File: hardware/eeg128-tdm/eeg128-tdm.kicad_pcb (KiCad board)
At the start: 4 copper layers, 190 x 110 mm, 642 parts, among them J1 J1, J10 J10, J11 J11, J2 J2, J3 J3, J4 J4, J5 J5, J6 J6, J7 J7, J8 J8, J9 TYPE-C-31-M-12, U1 U1, U10 U10, U11 U11, U12 U12, U13 U13, U14 U14, U15 U15, U16 U16, U17 U17, U18 U18, U19 U19, U2 U2, U20 U20, U21 U21, U22 U22, U23 U23, U24 U24, U25 U25, U26 U26, U27 U27, U3 U3, U4 U4, U5 U5, U6 U6, U7 U7, U8 U8, U9 U9, Y1 Y1

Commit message: Materialize generated KiCad schematic and release manifest
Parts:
- U21: footprint LQFP-32_5x5mm_P0.5mm -> TI_PBS_S-PQFP-G32_5x5mm_P0.5mm

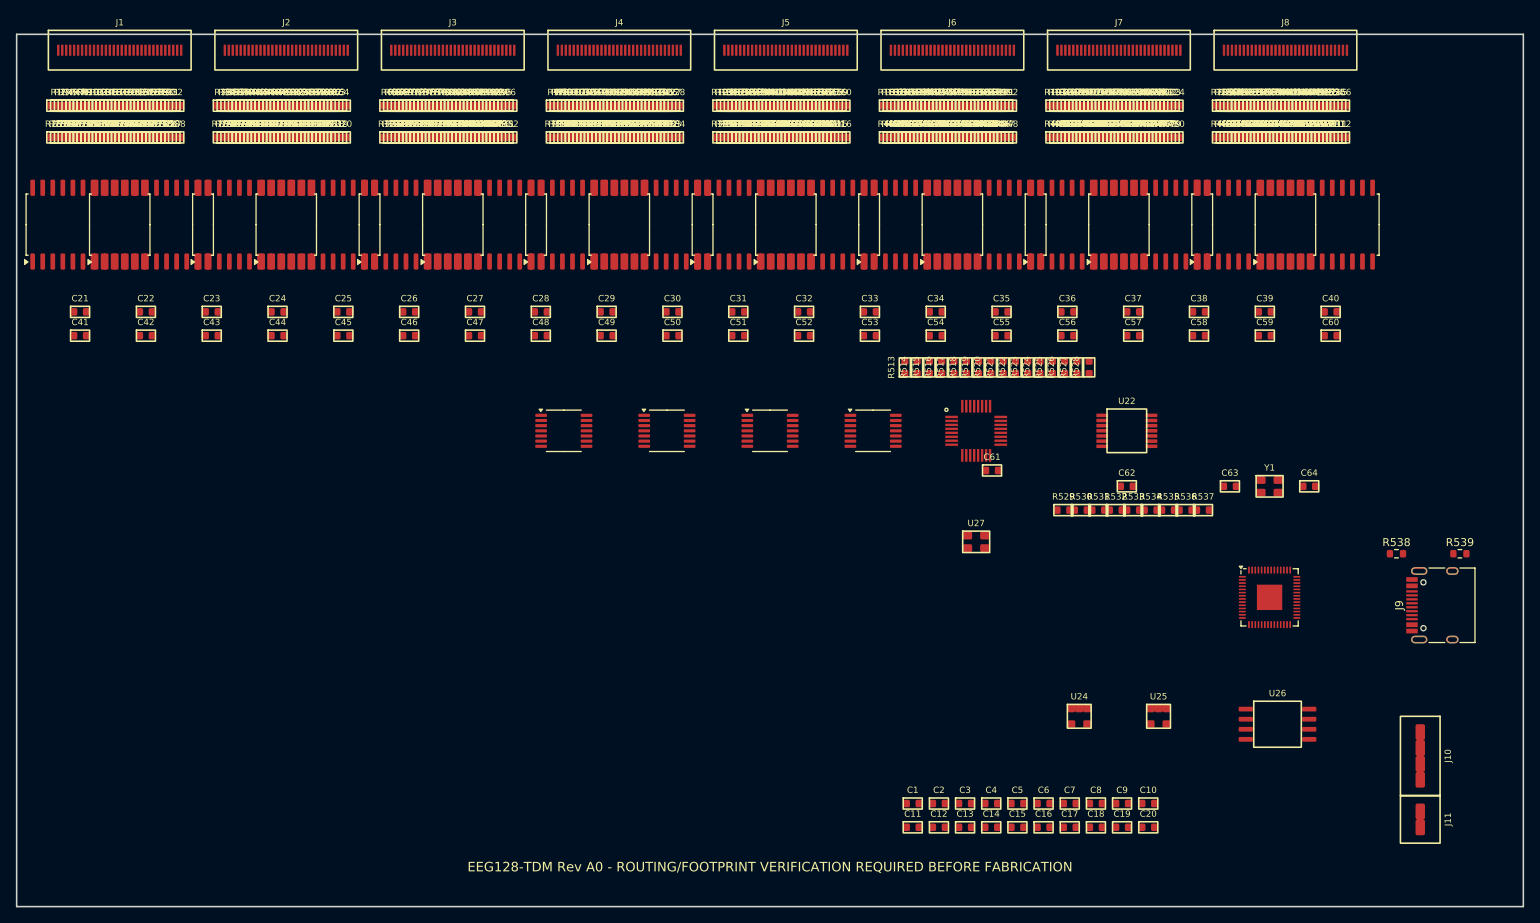
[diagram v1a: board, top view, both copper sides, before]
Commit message: Materialize verified pre-route PCB and gate primary geometry
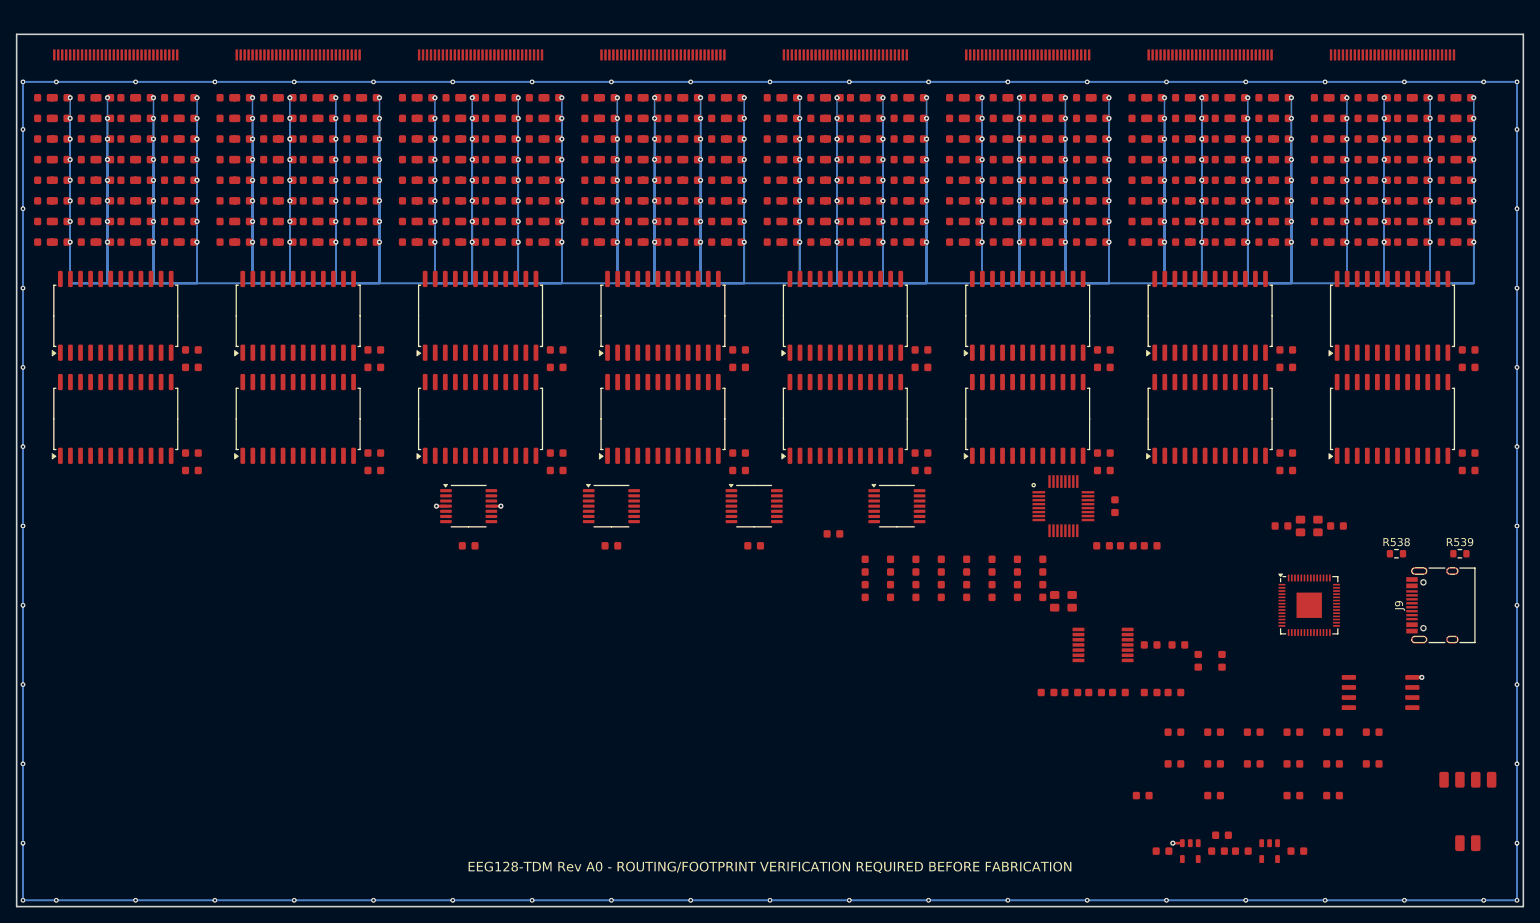
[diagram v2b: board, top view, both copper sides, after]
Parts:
- C1: footprint NBFM1_A0:C1 -> C1
- C10: footprint NBFM1_A0:C10 -> C10
- C11: footprint NBFM1_A0:C11 -> C11
- C12: footprint NBFM1_A0:C12 -> C12
- C13: footprint NBFM1_A0:C13 -> C13
- C14: footprint NBFM1_A0:C14 -> C14
- C15: footprint NBFM1_A0:C15 -> C15
- C16: footprint NBFM1_A0:C16 -> C16
- C17: footprint NBFM1_A0:C17 -> C17
- C18: footprint NBFM1_A0:C18 -> C18
- C19: footprint NBFM1_A0:C19 -> C19
- C2: footprint NBFM1_A0:C2 -> C2
- C20: footprint NBFM1_A0:C20 -> C20
- C21: footprint NBFM1_A0:C21 -> C21
- C22: footprint NBFM1_A0:C22 -> C22
- C23: footprint NBFM1_A0:C23 -> C23
- C24: footprint NBFM1_A0:C24 -> C24
- C25: footprint NBFM1_A0:C25 -> C25
- C26: footprint NBFM1_A0:C26 -> C26
- C27: footprint NBFM1_A0:C27 -> C27
- C28: footprint NBFM1_A0:C28 -> C28
- C29: footprint NBFM1_A0:C29 -> C29
- C3: footprint NBFM1_A0:C3 -> C3
- C30: footprint NBFM1_A0:C30 -> C30
- C31: footprint NBFM1_A0:C31 -> C31
- C32: footprint NBFM1_A0:C32 -> C32
- C33: footprint NBFM1_A0:C33 -> C33
- C34: footprint NBFM1_A0:C34 -> C34
- C35: footprint NBFM1_A0:C35 -> C35
- C36: footprint NBFM1_A0:C36 -> C36
- C37: footprint NBFM1_A0:C37 -> C37
- C38: footprint NBFM1_A0:C38 -> C38
- C39: footprint NBFM1_A0:C39 -> C39
- C4: footprint NBFM1_A0:C4 -> C4
- C40: footprint NBFM1_A0:C40 -> C40
- C41: footprint NBFM1_A0:C41 -> C41
- C42: footprint NBFM1_A0:C42 -> C42
- C43: footprint NBFM1_A0:C43 -> C43
- C44: footprint NBFM1_A0:C44 -> C44
- C45: footprint NBFM1_A0:C45 -> C45
- C46: footprint NBFM1_A0:C46 -> C46
- C47: footprint NBFM1_A0:C47 -> C47
- C48: footprint NBFM1_A0:C48 -> C48
- C49: footprint NBFM1_A0:C49 -> C49
- C5: footprint NBFM1_A0:C5 -> C5
- C50: footprint NBFM1_A0:C50 -> C50
- C51: footprint NBFM1_A0:C51 -> C51
- C52: footprint NBFM1_A0:C52 -> C52
- C53: footprint NBFM1_A0:C53 -> C53
- C54: footprint NBFM1_A0:C54 -> C54
- C55: footprint NBFM1_A0:C55 -> C55
- C56: footprint NBFM1_A0:C56 -> C56
- C57: footprint NBFM1_A0:C57 -> C57
- C58: footprint NBFM1_A0:C58 -> C58
- C59: footprint NBFM1_A0:C59 -> C59
- C6: footprint NBFM1_A0:C6 -> C6
- C60: footprint NBFM1_A0:C60 -> C60
- C61: footprint NBFM1_A0:C61 -> C61
- C62: footprint NBFM1_A0:C62 -> C62
- C63: footprint NBFM1_A0:C63 -> C63
- C64: footprint NBFM1_A0:C64 -> C64
- C7: footprint NBFM1_A0:C7 -> C7
- C8: footprint NBFM1_A0:C8 -> C8
- C9: footprint NBFM1_A0:C9 -> C9
- J1: footprint NBFM1_A0:J1 -> J1
- J10: footprint NBFM1_A0:J10 -> J10
- J11: footprint NBFM1_A0:J11 -> J11
- J2: footprint NBFM1_A0:J2 -> J2
- J3: footprint NBFM1_A0:J3 -> J3
- J4: footprint NBFM1_A0:J4 -> J4
- J5: footprint NBFM1_A0:J5 -> J5
- J6: footprint NBFM1_A0:J6 -> J6
- J7: footprint NBFM1_A0:J7 -> J7
- J8: footprint NBFM1_A0:J8 -> J8
- R1: footprint NBFM1_A0:R1 -> R1
- R10: footprint NBFM1_A0:R10 -> R10
- R100: footprint NBFM1_A0:R100 -> R100
- R101: footprint NBFM1_A0:R101 -> R101
- R102: footprint NBFM1_A0:R102 -> R102
- R103: footprint NBFM1_A0:R103 -> R103
- R104: footprint NBFM1_A0:R104 -> R104
- R105: footprint NBFM1_A0:R105 -> R105
- R106: footprint NBFM1_A0:R106 -> R106
- R107: footprint NBFM1_A0:R107 -> R107
- R108: footprint NBFM1_A0:R108 -> R108
- R109: footprint NBFM1_A0:R109 -> R109
- R11: footprint NBFM1_A0:R11 -> R11
- R110: footprint NBFM1_A0:R110 -> R110
- R111: footprint NBFM1_A0:R111 -> R111
- R112: footprint NBFM1_A0:R112 -> R112
- R113: footprint NBFM1_A0:R113 -> R113
- R114: footprint NBFM1_A0:R114 -> R114
- R115: footprint NBFM1_A0:R115 -> R115
- R116: footprint NBFM1_A0:R116 -> R116
- R117: footprint NBFM1_A0:R117 -> R117
- R118: footprint NBFM1_A0:R118 -> R118
- R119: footprint NBFM1_A0:R119 -> R119
- R12: footprint NBFM1_A0:R12 -> R12
- R120: footprint NBFM1_A0:R120 -> R120
- R121: footprint NBFM1_A0:R121 -> R121
- R122: footprint NBFM1_A0:R122 -> R122
- R123: footprint NBFM1_A0:R123 -> R123
- R124: footprint NBFM1_A0:R124 -> R124
- R125: footprint NBFM1_A0:R125 -> R125
- R126: footprint NBFM1_A0:R126 -> R126
- R127: footprint NBFM1_A0:R127 -> R127
- R128: footprint NBFM1_A0:R128 -> R128
- R129: footprint NBFM1_A0:R129 -> R129
- R13: footprint NBFM1_A0:R13 -> R13
- R130: footprint NBFM1_A0:R130 -> R130
- R131: footprint NBFM1_A0:R131 -> R131
- R132: footprint NBFM1_A0:R132 -> R132
- R133: footprint NBFM1_A0:R133 -> R133
- R134: footprint NBFM1_A0:R134 -> R134
- R135: footprint NBFM1_A0:R135 -> R135
- R136: footprint NBFM1_A0:R136 -> R136
- R137: footprint NBFM1_A0:R137 -> R137
- R138: footprint NBFM1_A0:R138 -> R138
- R139: footprint NBFM1_A0:R139 -> R139
- R14: footprint NBFM1_A0:R14 -> R14
- R140: footprint NBFM1_A0:R140 -> R140
- R141: footprint NBFM1_A0:R141 -> R141
- R142: footprint NBFM1_A0:R142 -> R142
- R143: footprint NBFM1_A0:R143 -> R143
- R144: footprint NBFM1_A0:R144 -> R144
- R145: footprint NBFM1_A0:R145 -> R145
- R146: footprint NBFM1_A0:R146 -> R146
- R147: footprint NBFM1_A0:R147 -> R147
- R148: footprint NBFM1_A0:R148 -> R148
- R149: footprint NBFM1_A0:R149 -> R149
- R15: footprint NBFM1_A0:R15 -> R15
- R150: footprint NBFM1_A0:R150 -> R150
- R151: footprint NBFM1_A0:R151 -> R151
- R152: footprint NBFM1_A0:R152 -> R152
- R153: footprint NBFM1_A0:R153 -> R153
- R154: footprint NBFM1_A0:R154 -> R154
- R155: footprint NBFM1_A0:R155 -> R155
- R156: footprint NBFM1_A0:R156 -> R156
- R157: footprint NBFM1_A0:R157 -> R157
- R158: footprint NBFM1_A0:R158 -> R158
- R159: footprint NBFM1_A0:R159 -> R159
- R16: footprint NBFM1_A0:R16 -> R16
- R160: footprint NBFM1_A0:R160 -> R160
- R161: footprint NBFM1_A0:R161 -> R161
- R162: footprint NBFM1_A0:R162 -> R162
- R163: footprint NBFM1_A0:R163 -> R163
- R164: footprint NBFM1_A0:R164 -> R164
- R165: footprint NBFM1_A0:R165 -> R165
- R166: footprint NBFM1_A0:R166 -> R166
- R167: footprint NBFM1_A0:R167 -> R167
- R168: footprint NBFM1_A0:R168 -> R168
- R169: footprint NBFM1_A0:R169 -> R169
- R17: footprint NBFM1_A0:R17 -> R17
- R170: footprint NBFM1_A0:R170 -> R170
- R171: footprint NBFM1_A0:R171 -> R171
- R172: footprint NBFM1_A0:R172 -> R172
- R173: footprint NBFM1_A0:R173 -> R173
- R174: footprint NBFM1_A0:R174 -> R174
- R175: footprint NBFM1_A0:R175 -> R175
- R176: footprint NBFM1_A0:R176 -> R176
- R177: footprint NBFM1_A0:R177 -> R177
- R178: footprint NBFM1_A0:R178 -> R178
- R179: footprint NBFM1_A0:R179 -> R179
- R18: footprint NBFM1_A0:R18 -> R18
- R180: footprint NBFM1_A0:R180 -> R180
- R181: footprint NBFM1_A0:R181 -> R181
- R182: footprint NBFM1_A0:R182 -> R182
- R183: footprint NBFM1_A0:R183 -> R183
- R184: footprint NBFM1_A0:R184 -> R184
- R185: footprint NBFM1_A0:R185 -> R185
- R186: footprint NBFM1_A0:R186 -> R186
- R187: footprint NBFM1_A0:R187 -> R187
- R188: footprint NBFM1_A0:R188 -> R188
- R189: footprint NBFM1_A0:R189 -> R189
- R19: footprint NBFM1_A0:R19 -> R19
- R190: footprint NBFM1_A0:R190 -> R190
- R191: footprint NBFM1_A0:R191 -> R191
- R192: footprint NBFM1_A0:R192 -> R192
- R193: footprint NBFM1_A0:R193 -> R193
- R194: footprint NBFM1_A0:R194 -> R194
- R195: footprint NBFM1_A0:R195 -> R195
- R196: footprint NBFM1_A0:R196 -> R196
- R197: footprint NBFM1_A0:R197 -> R197
- R198: footprint NBFM1_A0:R198 -> R198
- R199: footprint NBFM1_A0:R199 -> R199
- R2: footprint NBFM1_A0:R2 -> R2
- R20: footprint NBFM1_A0:R20 -> R20
- R200: footprint NBFM1_A0:R200 -> R200
- R201: footprint NBFM1_A0:R201 -> R201
- R202: footprint NBFM1_A0:R202 -> R202
- R203: footprint NBFM1_A0:R203 -> R203
- R204: footprint NBFM1_A0:R204 -> R204
- R205: footprint NBFM1_A0:R205 -> R205
- R206: footprint NBFM1_A0:R206 -> R206
- R207: footprint NBFM1_A0:R207 -> R207
- R208: footprint NBFM1_A0:R208 -> R208
- R209: footprint NBFM1_A0:R209 -> R209
- R21: footprint NBFM1_A0:R21 -> R21
- R210: footprint NBFM1_A0:R210 -> R210
- R211: footprint NBFM1_A0:R211 -> R211
- R212: footprint NBFM1_A0:R212 -> R212
- R213: footprint NBFM1_A0:R213 -> R213
- R214: footprint NBFM1_A0:R214 -> R214
- R215: footprint NBFM1_A0:R215 -> R215
- R216: footprint NBFM1_A0:R216 -> R216
- R217: footprint NBFM1_A0:R217 -> R217
- R218: footprint NBFM1_A0:R218 -> R218
- R219: footprint NBFM1_A0:R219 -> R219
- R22: footprint NBFM1_A0:R22 -> R22
- R220: footprint NBFM1_A0:R220 -> R220
- R221: footprint NBFM1_A0:R221 -> R221
- R222: footprint NBFM1_A0:R222 -> R222
- R223: footprint NBFM1_A0:R223 -> R223
- R224: footprint NBFM1_A0:R224 -> R224
- R225: footprint NBFM1_A0:R225 -> R225
- R226: footprint NBFM1_A0:R226 -> R226
- R227: footprint NBFM1_A0:R227 -> R227
- R228: footprint NBFM1_A0:R228 -> R228
- R229: footprint NBFM1_A0:R229 -> R229
- R23: footprint NBFM1_A0:R23 -> R23
- R230: footprint NBFM1_A0:R230 -> R230
- R231: footprint NBFM1_A0:R231 -> R231
- R232: footprint NBFM1_A0:R232 -> R232
- R233: footprint NBFM1_A0:R233 -> R233
- R234: footprint NBFM1_A0:R234 -> R234
- R235: footprint NBFM1_A0:R235 -> R235
- R236: footprint NBFM1_A0:R236 -> R236
- R237: footprint NBFM1_A0:R237 -> R237
- R238: footprint NBFM1_A0:R238 -> R238
- R239: footprint NBFM1_A0:R239 -> R239
- R24: footprint NBFM1_A0:R24 -> R24
- R240: footprint NBFM1_A0:R240 -> R240
- R241: footprint NBFM1_A0:R241 -> R241
- R242: footprint NBFM1_A0:R242 -> R242
- R243: footprint NBFM1_A0:R243 -> R243
- R244: footprint NBFM1_A0:R244 -> R244
- R245: footprint NBFM1_A0:R245 -> R245
- R246: footprint NBFM1_A0:R246 -> R246
- R247: footprint NBFM1_A0:R247 -> R247
- R248: footprint NBFM1_A0:R248 -> R248
- R249: footprint NBFM1_A0:R249 -> R249
- R25: footprint NBFM1_A0:R25 -> R25
- R250: footprint NBFM1_A0:R250 -> R250
- R251: footprint NBFM1_A0:R251 -> R251
- R252: footprint NBFM1_A0:R252 -> R252
- R253: footprint NBFM1_A0:R253 -> R253
- R254: footprint NBFM1_A0:R254 -> R254
- R255: footprint NBFM1_A0:R255 -> R255
- R256: footprint NBFM1_A0:R256 -> R256
- R257: footprint NBFM1_A0:R257 -> R257
- R258: footprint NBFM1_A0:R258 -> R258
- R259: footprint NBFM1_A0:R259 -> R259
- R26: footprint NBFM1_A0:R26 -> R26
- R260: footprint NBFM1_A0:R260 -> R260
- R261: footprint NBFM1_A0:R261 -> R261
- R262: footprint NBFM1_A0:R262 -> R262
- R263: footprint NBFM1_A0:R263 -> R263
- R264: footprint NBFM1_A0:R264 -> R264
- R265: footprint NBFM1_A0:R265 -> R265
- R266: footprint NBFM1_A0:R266 -> R266
- R267: footprint NBFM1_A0:R267 -> R267
- R268: footprint NBFM1_A0:R268 -> R268
- R269: footprint NBFM1_A0:R269 -> R269
- R27: footprint NBFM1_A0:R27 -> R27
- R270: footprint NBFM1_A0:R270 -> R270
- R271: footprint NBFM1_A0:R271 -> R271
- R272: footprint NBFM1_A0:R272 -> R272
- R273: footprint NBFM1_A0:R273 -> R273
- R274: footprint NBFM1_A0:R274 -> R274
- R275: footprint NBFM1_A0:R275 -> R275
- R276: footprint NBFM1_A0:R276 -> R276
- R277: footprint NBFM1_A0:R277 -> R277
- R278: footprint NBFM1_A0:R278 -> R278
- R279: footprint NBFM1_A0:R279 -> R279
- R28: footprint NBFM1_A0:R28 -> R28
- R280: footprint NBFM1_A0:R280 -> R280
- R281: footprint NBFM1_A0:R281 -> R281
- R282: footprint NBFM1_A0:R282 -> R282
- R283: footprint NBFM1_A0:R283 -> R283
- R284: footprint NBFM1_A0:R284 -> R284
- R285: footprint NBFM1_A0:R285 -> R285
- R286: footprint NBFM1_A0:R286 -> R286
- R287: footprint NBFM1_A0:R287 -> R287
- R288: footprint NBFM1_A0:R288 -> R288
- R289: footprint NBFM1_A0:R289 -> R289
- R29: footprint NBFM1_A0:R29 -> R29
- R290: footprint NBFM1_A0:R290 -> R290
- R291: footprint NBFM1_A0:R291 -> R291
- R292: footprint NBFM1_A0:R292 -> R292
- R293: footprint NBFM1_A0:R293 -> R293
- R294: footprint NBFM1_A0:R294 -> R294
- R295: footprint NBFM1_A0:R295 -> R295
- R296: footprint NBFM1_A0:R296 -> R296
- R297: footprint NBFM1_A0:R297 -> R297
- R298: footprint NBFM1_A0:R298 -> R298
- R299: footprint NBFM1_A0:R299 -> R299
- R3: footprint NBFM1_A0:R3 -> R3
- R30: footprint NBFM1_A0:R30 -> R30
- R300: footprint NBFM1_A0:R300 -> R300
- R301: footprint NBFM1_A0:R301 -> R301
- R302: footprint NBFM1_A0:R302 -> R302
- R303: footprint NBFM1_A0:R303 -> R303
- R304: footprint NBFM1_A0:R304 -> R304
- R305: footprint NBFM1_A0:R305 -> R305
- R306: footprint NBFM1_A0:R306 -> R306
- R307: footprint NBFM1_A0:R307 -> R307
- R308: footprint NBFM1_A0:R308 -> R308
- R309: footprint NBFM1_A0:R309 -> R309
- R31: footprint NBFM1_A0:R31 -> R31
- R310: footprint NBFM1_A0:R310 -> R310
- R311: footprint NBFM1_A0:R311 -> R311
- R312: footprint NBFM1_A0:R312 -> R312
- R313: footprint NBFM1_A0:R313 -> R313
- R314: footprint NBFM1_A0:R314 -> R314
- R315: footprint NBFM1_A0:R315 -> R315
- R316: footprint NBFM1_A0:R316 -> R316
- R317: footprint NBFM1_A0:R317 -> R317
- R318: footprint NBFM1_A0:R318 -> R318
- R319: footprint NBFM1_A0:R319 -> R319
- R32: footprint NBFM1_A0:R32 -> R32
- R320: footprint NBFM1_A0:R320 -> R320
- R321: footprint NBFM1_A0:R321 -> R321
- R322: footprint NBFM1_A0:R322 -> R322
- R323: footprint NBFM1_A0:R323 -> R323
- R324: footprint NBFM1_A0:R324 -> R324
- R325: footprint NBFM1_A0:R325 -> R325
- R326: footprint NBFM1_A0:R326 -> R326
- R327: footprint NBFM1_A0:R327 -> R327
- R328: footprint NBFM1_A0:R328 -> R328
- R329: footprint NBFM1_A0:R329 -> R329
- R33: footprint NBFM1_A0:R33 -> R33
- R330: footprint NBFM1_A0:R330 -> R330
- R331: footprint NBFM1_A0:R331 -> R331
- R332: footprint NBFM1_A0:R332 -> R332
- R333: footprint NBFM1_A0:R333 -> R333
- R334: footprint NBFM1_A0:R334 -> R334
- R335: footprint NBFM1_A0:R335 -> R335
- R336: footprint NBFM1_A0:R336 -> R336
- R337: footprint NBFM1_A0:R337 -> R337
- R338: footprint NBFM1_A0:R338 -> R338
- R339: footprint NBFM1_A0:R339 -> R339
- R34: footprint NBFM1_A0:R34 -> R34
- R340: footprint NBFM1_A0:R340 -> R340
- R341: footprint NBFM1_A0:R341 -> R341
- R342: footprint NBFM1_A0:R342 -> R342
- R343: footprint NBFM1_A0:R343 -> R343
- R344: footprint NBFM1_A0:R344 -> R344
- R345: footprint NBFM1_A0:R345 -> R345
- R346: footprint NBFM1_A0:R346 -> R346
- R347: footprint NBFM1_A0:R347 -> R347
- R348: footprint NBFM1_A0:R348 -> R348
- R349: footprint NBFM1_A0:R349 -> R349
- R35: footprint NBFM1_A0:R35 -> R35
- R350: footprint NBFM1_A0:R350 -> R350
- R351: footprint NBFM1_A0:R351 -> R351
- R352: footprint NBFM1_A0:R352 -> R352
- R353: footprint NBFM1_A0:R353 -> R353
- R354: footprint NBFM1_A0:R354 -> R354
- R355: footprint NBFM1_A0:R355 -> R355
- R356: footprint NBFM1_A0:R356 -> R356
- R357: footprint NBFM1_A0:R357 -> R357
- R358: footprint NBFM1_A0:R358 -> R358
- R359: footprint NBFM1_A0:R359 -> R359
- R36: footprint NBFM1_A0:R36 -> R36
- R360: footprint NBFM1_A0:R360 -> R360
- R361: footprint NBFM1_A0:R361 -> R361
- R362: footprint NBFM1_A0:R362 -> R362
- R363: footprint NBFM1_A0:R363 -> R363
- R364: footprint NBFM1_A0:R364 -> R364
- R365: footprint NBFM1_A0:R365 -> R365
- R366: footprint NBFM1_A0:R366 -> R366
- R367: footprint NBFM1_A0:R367 -> R367
- R368: footprint NBFM1_A0:R368 -> R368
- R369: footprint NBFM1_A0:R369 -> R369
- R37: footprint NBFM1_A0:R37 -> R37
- R370: footprint NBFM1_A0:R370 -> R370
- R371: footprint NBFM1_A0:R371 -> R371
- R372: footprint NBFM1_A0:R372 -> R372
- R373: footprint NBFM1_A0:R373 -> R373
- R374: footprint NBFM1_A0:R374 -> R374
- R375: footprint NBFM1_A0:R375 -> R375
- R376: footprint NBFM1_A0:R376 -> R376
- R377: footprint NBFM1_A0:R377 -> R377
- R378: footprint NBFM1_A0:R378 -> R378
- R379: footprint NBFM1_A0:R379 -> R379
- R38: footprint NBFM1_A0:R38 -> R38
- R380: footprint NBFM1_A0:R380 -> R380
- R381: footprint NBFM1_A0:R381 -> R381
- R382: footprint NBFM1_A0:R382 -> R382
- R383: footprint NBFM1_A0:R383 -> R383
- R384: footprint NBFM1_A0:R384 -> R384
- R385: footprint NBFM1_A0:R385 -> R385
- R386: footprint NBFM1_A0:R386 -> R386
- R387: footprint NBFM1_A0:R387 -> R387
- R388: footprint NBFM1_A0:R388 -> R388
- R389: footprint NBFM1_A0:R389 -> R389
- R39: footprint NBFM1_A0:R39 -> R39
- R390: footprint NBFM1_A0:R390 -> R390
- R391: footprint NBFM1_A0:R391 -> R391
- R392: footprint NBFM1_A0:R392 -> R392
- R393: footprint NBFM1_A0:R393 -> R393
- R394: footprint NBFM1_A0:R394 -> R394
- R395: footprint NBFM1_A0:R395 -> R395
- R396: footprint NBFM1_A0:R396 -> R396
- R397: footprint NBFM1_A0:R397 -> R397
- R398: footprint NBFM1_A0:R398 -> R398
- R399: footprint NBFM1_A0:R399 -> R399
- R4: footprint NBFM1_A0:R4 -> R4
- R40: footprint NBFM1_A0:R40 -> R40
- R400: footprint NBFM1_A0:R400 -> R400
- R401: footprint NBFM1_A0:R401 -> R401
- R402: footprint NBFM1_A0:R402 -> R402
- R403: footprint NBFM1_A0:R403 -> R403
- R404: footprint NBFM1_A0:R404 -> R404
- R405: footprint NBFM1_A0:R405 -> R405
- R406: footprint NBFM1_A0:R406 -> R406
- R407: footprint NBFM1_A0:R407 -> R407
- R408: footprint NBFM1_A0:R408 -> R408
- R409: footprint NBFM1_A0:R409 -> R409
- R41: footprint NBFM1_A0:R41 -> R41
- R410: footprint NBFM1_A0:R410 -> R410
- R411: footprint NBFM1_A0:R411 -> R411
- R412: footprint NBFM1_A0:R412 -> R412
- R413: footprint NBFM1_A0:R413 -> R413
- R414: footprint NBFM1_A0:R414 -> R414
- R415: footprint NBFM1_A0:R415 -> R415
- R416: footprint NBFM1_A0:R416 -> R416
- R417: footprint NBFM1_A0:R417 -> R417
- R418: footprint NBFM1_A0:R418 -> R418
- R419: footprint NBFM1_A0:R419 -> R419
- R42: footprint NBFM1_A0:R42 -> R42
- R420: footprint NBFM1_A0:R420 -> R420
- R421: footprint NBFM1_A0:R421 -> R421
- R422: footprint NBFM1_A0:R422 -> R422
- R423: footprint NBFM1_A0:R423 -> R423
- R424: footprint NBFM1_A0:R424 -> R424
- R425: footprint NBFM1_A0:R425 -> R425
- R426: footprint NBFM1_A0:R426 -> R426
- R427: footprint NBFM1_A0:R427 -> R427
- R428: footprint NBFM1_A0:R428 -> R428
- R429: footprint NBFM1_A0:R429 -> R429
- R43: footprint NBFM1_A0:R43 -> R43
- R430: footprint NBFM1_A0:R430 -> R430
- R431: footprint NBFM1_A0:R431 -> R431
- R432: footprint NBFM1_A0:R432 -> R432
- R433: footprint NBFM1_A0:R433 -> R433
- R434: footprint NBFM1_A0:R434 -> R434
- R435: footprint NBFM1_A0:R435 -> R435
- R436: footprint NBFM1_A0:R436 -> R436
- R437: footprint NBFM1_A0:R437 -> R437
- R438: footprint NBFM1_A0:R438 -> R438
- R439: footprint NBFM1_A0:R439 -> R439
- R44: footprint NBFM1_A0:R44 -> R44
- R440: footprint NBFM1_A0:R440 -> R440
- R441: footprint NBFM1_A0:R441 -> R441
- R442: footprint NBFM1_A0:R442 -> R442
- R443: footprint NBFM1_A0:R443 -> R443
- R444: footprint NBFM1_A0:R444 -> R444
- R445: footprint NBFM1_A0:R445 -> R445
- R446: footprint NBFM1_A0:R446 -> R446
- R447: footprint NBFM1_A0:R447 -> R447
- R448: footprint NBFM1_A0:R448 -> R448
- R449: footprint NBFM1_A0:R449 -> R449
- R45: footprint NBFM1_A0:R45 -> R45
- R450: footprint NBFM1_A0:R450 -> R450
- R451: footprint NBFM1_A0:R451 -> R451
- R452: footprint NBFM1_A0:R452 -> R452
- R453: footprint NBFM1_A0:R453 -> R453
- R454: footprint NBFM1_A0:R454 -> R454
- R455: footprint NBFM1_A0:R455 -> R455
- R456: footprint NBFM1_A0:R456 -> R456
- R457: footprint NBFM1_A0:R457 -> R457
- R458: footprint NBFM1_A0:R458 -> R458
- R459: footprint NBFM1_A0:R459 -> R459
- R46: footprint NBFM1_A0:R46 -> R46
- R460: footprint NBFM1_A0:R460 -> R460
- R461: footprint NBFM1_A0:R461 -> R461
- R462: footprint NBFM1_A0:R462 -> R462
- R463: footprint NBFM1_A0:R463 -> R463
- R464: footprint NBFM1_A0:R464 -> R464
- R465: footprint NBFM1_A0:R465 -> R465
- R466: footprint NBFM1_A0:R466 -> R466
- R467: footprint NBFM1_A0:R467 -> R467
- R468: footprint NBFM1_A0:R468 -> R468
- R469: footprint NBFM1_A0:R469 -> R469
- R47: footprint NBFM1_A0:R47 -> R47
- R470: footprint NBFM1_A0:R470 -> R470
- R471: footprint NBFM1_A0:R471 -> R471
- R472: footprint NBFM1_A0:R472 -> R472
- R473: footprint NBFM1_A0:R473 -> R473
- R474: footprint NBFM1_A0:R474 -> R474
- R475: footprint NBFM1_A0:R475 -> R475
- R476: footprint NBFM1_A0:R476 -> R476
- R477: footprint NBFM1_A0:R477 -> R477
- R478: footprint NBFM1_A0:R478 -> R478
- R479: footprint NBFM1_A0:R479 -> R479
- R48: footprint NBFM1_A0:R48 -> R48
- R480: footprint NBFM1_A0:R480 -> R480
- R481: footprint NBFM1_A0:R481 -> R481
- R482: footprint NBFM1_A0:R482 -> R482
- R483: footprint NBFM1_A0:R483 -> R483
- R484: footprint NBFM1_A0:R484 -> R484
- R485: footprint NBFM1_A0:R485 -> R485
- R486: footprint NBFM1_A0:R486 -> R486
- R487: footprint NBFM1_A0:R487 -> R487
- R488: footprint NBFM1_A0:R488 -> R488
- R489: footprint NBFM1_A0:R489 -> R489
- R49: footprint NBFM1_A0:R49 -> R49
- R490: footprint NBFM1_A0:R490 -> R490
- R491: footprint NBFM1_A0:R491 -> R491
- R492: footprint NBFM1_A0:R492 -> R492
- R493: footprint NBFM1_A0:R493 -> R493
- R494: footprint NBFM1_A0:R494 -> R494
- R495: footprint NBFM1_A0:R495 -> R495
- R496: footprint NBFM1_A0:R496 -> R496
- R497: footprint NBFM1_A0:R497 -> R497
- R498: footprint NBFM1_A0:R498 -> R498
- R499: footprint NBFM1_A0:R499 -> R499
- R5: footprint NBFM1_A0:R5 -> R5
- R50: footprint NBFM1_A0:R50 -> R50
- R500: footprint NBFM1_A0:R500 -> R500
- R501: footprint NBFM1_A0:R501 -> R501
- R502: footprint NBFM1_A0:R502 -> R502
- R503: footprint NBFM1_A0:R503 -> R503
- R504: footprint NBFM1_A0:R504 -> R504
- R505: footprint NBFM1_A0:R505 -> R505
- R506: footprint NBFM1_A0:R506 -> R506
- R507: footprint NBFM1_A0:R507 -> R507
- R508: footprint NBFM1_A0:R508 -> R508
- R509: footprint NBFM1_A0:R509 -> R509
- R51: footprint NBFM1_A0:R51 -> R51
- R510: footprint NBFM1_A0:R510 -> R510
- R511: footprint NBFM1_A0:R511 -> R511
- R512: footprint NBFM1_A0:R512 -> R512
- R513: footprint NBFM1_A0:R513 -> R513
- R514: footprint NBFM1_A0:R514 -> R514
- R515: footprint NBFM1_A0:R515 -> R515
- R516: footprint NBFM1_A0:R516 -> R516
- R517: footprint NBFM1_A0:R517 -> R517
- R518: footprint NBFM1_A0:R518 -> R518
- R519: footprint NBFM1_A0:R519 -> R519
- R52: footprint NBFM1_A0:R52 -> R52
- R520: footprint NBFM1_A0:R520 -> R520
- R521: footprint NBFM1_A0:R521 -> R521
- R522: footprint NBFM1_A0:R522 -> R522
- R523: footprint NBFM1_A0:R523 -> R523
- R524: footprint NBFM1_A0:R524 -> R524
- R525: footprint NBFM1_A0:R525 -> R525
- R526: footprint NBFM1_A0:R526 -> R526
- R527: footprint NBFM1_A0:R527 -> R527
- R528: footprint NBFM1_A0:R528 -> R528
- R529: footprint NBFM1_A0:R529 -> R529
- R53: footprint NBFM1_A0:R53 -> R53
- R530: footprint NBFM1_A0:R530 -> R530
- R531: footprint NBFM1_A0:R531 -> R531
- R532: footprint NBFM1_A0:R532 -> R532
- R533: footprint NBFM1_A0:R533 -> R533
- R534: footprint NBFM1_A0:R534 -> R534
- R535: footprint NBFM1_A0:R535 -> R535
- R536: footprint NBFM1_A0:R536 -> R536
- R537: footprint NBFM1_A0:R537 -> R537
- R54: footprint NBFM1_A0:R54 -> R54
- R55: footprint NBFM1_A0:R55 -> R55
- R56: footprint NBFM1_A0:R56 -> R56
- R57: footprint NBFM1_A0:R57 -> R57
- R58: footprint NBFM1_A0:R58 -> R58
- R59: footprint NBFM1_A0:R59 -> R59
- R6: footprint NBFM1_A0:R6 -> R6
- R60: footprint NBFM1_A0:R60 -> R60
- R61: footprint NBFM1_A0:R61 -> R61
- R62: footprint NBFM1_A0:R62 -> R62
- R63: footprint NBFM1_A0:R63 -> R63
- R64: footprint NBFM1_A0:R64 -> R64
- R65: footprint NBFM1_A0:R65 -> R65
- R66: footprint NBFM1_A0:R66 -> R66
- R67: footprint NBFM1_A0:R67 -> R67
- R68: footprint NBFM1_A0:R68 -> R68
- R69: footprint NBFM1_A0:R69 -> R69
- R7: footprint NBFM1_A0:R7 -> R7
- R70: footprint NBFM1_A0:R70 -> R70
- R71: footprint NBFM1_A0:R71 -> R71
- R72: footprint NBFM1_A0:R72 -> R72
- R73: footprint NBFM1_A0:R73 -> R73
- R74: footprint NBFM1_A0:R74 -> R74
- R75: footprint NBFM1_A0:R75 -> R75
- R76: footprint NBFM1_A0:R76 -> R76
- R77: footprint NBFM1_A0:R77 -> R77
- R78: footprint NBFM1_A0:R78 -> R78
- R79: footprint NBFM1_A0:R79 -> R79
- R8: footprint NBFM1_A0:R8 -> R8
- R80: footprint NBFM1_A0:R80 -> R80
- R81: footprint NBFM1_A0:R81 -> R81
- R82: footprint NBFM1_A0:R82 -> R82
- R83: footprint NBFM1_A0:R83 -> R83
- R84: footprint NBFM1_A0:R84 -> R84
- R85: footprint NBFM1_A0:R85 -> R85
- R86: footprint NBFM1_A0:R86 -> R86
- R87: footprint NBFM1_A0:R87 -> R87
- R88: footprint NBFM1_A0:R88 -> R88
- R89: footprint NBFM1_A0:R89 -> R89
- R9: footprint NBFM1_A0:R9 -> R9
- R90: footprint NBFM1_A0:R90 -> R90
- R91: footprint NBFM1_A0:R91 -> R91
- R92: footprint NBFM1_A0:R92 -> R92
- R93: footprint NBFM1_A0:R93 -> R93
- R94: footprint NBFM1_A0:R94 -> R94
- R95: footprint NBFM1_A0:R95 -> R95
- R96: footprint NBFM1_A0:R96 -> R96
- R97: footprint NBFM1_A0:R97 -> R97
- R98: footprint NBFM1_A0:R98 -> R98
- R99: footprint NBFM1_A0:R99 -> R99
- U22: footprint NBFM1_A0:U22 -> U22
- U24: footprint NBFM1_A0:U24 -> U24
- U25: footprint NBFM1_A0:U25 -> U25
- U26: footprint NBFM1_A0:U26 -> U26
- U27: footprint NBFM1_A0:U27 -> U27
- Y1: footprint NBFM1_A0:Y1 -> Y1
- moved C41 131.7 mm to (142.0, 69.5)
- moved C42 126.5 mm to (145.0, 69.5)
- moved C44 123.7 mm to (151.0, 93.0)
- moved C43 121.3 mm to (148.0, 69.5)
- moved C45 120.6 mm to (156.0, 93.0)
- moved C46 117.7 mm to (161.0, 93.0)
- moved C47 114.7 mm to (166.0, 93.0)
- moved C48 111.7 mm to (171.0, 93.0)
- moved C49 108.8 mm to (176.0, 93.0)
- moved C1 107.4 mm to (27.1, 44.8)
- moved C2 104.1 mm to (27.1, 57.8)
- moved C3 93.9 mm to (50.1, 44.8)
- moved C4 89.5 mm to (50.1, 57.8)
- moved C37 88.8 mm to (62.0, 69.5)
- moved C50 83.2 mm to (151.0, 97.0)
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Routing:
- net VCM: track 0.00 -> 4068.2 mm, vias 0 -> 256
- net AGND: track 0.00 -> 584.4 mm, vias 0 -> 63
- net 3V3A: track 0.00 -> 1.20 mm, vias 0 -> 1
- net 5V_ISO: track 0.00 -> 1.20 mm, vias 0 -> 1
- net 3V3D: track 0.00 -> 1.20 mm, vias 0 -> 1
- net CH095_P_MUX: track 0.00 -> 0.50 mm
- net CH094_P_MUX: track 0.00 -> 0.50 mm
- net CH093_P_MUX: track 0.00 -> 0.50 mm
- net CH092_P_MUX: track 0.00 -> 0.50 mm
- net CH091_P_MUX: track 0.00 -> 0.50 mm
- net CH090_P_MUX: track 0.00 -> 0.50 mm
- net CH089_P_MUX: track 0.00 -> 0.50 mm
- net CH088_P_MUX: track 0.00 -> 0.50 mm
- net CH087_N_MUX: track 0.00 -> 0.50 mm
- net CH086_N_MUX: track 0.00 -> 0.50 mm
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- added copper zone on In2.Cu, net 3V3A
- added copper zone on In2.Cu, net 3V3D
- added copper zone on In2.Cu, net 5V_ISO
- added copper zone on In1.Cu, net AGND
